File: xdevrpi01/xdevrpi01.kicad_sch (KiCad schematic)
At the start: 20 parts

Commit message: xdevrpi01
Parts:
- removed C?: 22uF, symbol Device:C
- removed U?: AMS1117-3.3, Package_TO_SOT_SMD:SOT-223-3_TabPin2, symbol Regulator_Linear:AMS1117-3.3
- added C1, C2: 15pF, Capacitor_SMD:C_0402_1005Metric, symbol Device:C
- added C3, C4, C5: 100nF, Capacitor_SMD:C_0402_1005Metric, symbol Device:C
- added C6, C7: 1uF, Capacitor_SMD:C_0402_1005Metric, symbol Device:C
- added D1: LED, LED_SMD:LED_0603_1608Metric, symbol Device:LED
- added R1, R2: 27, Resistor_SMD:R_0402_1005Metric, symbol Device:R
- added R3, R4, R6: 1k, Resistor_SMD:R_0402_1005Metric, symbol Device:R
- added R5, R9: 10k, Resistor_SMD:R_0402_1005Metric, symbol Device:R
- added SW1: BOOT, tactile_switches:TS-1088-AR02016, symbol Switch:SW_Push
- added SW2: RST, tactile_switches:TS-1088-AR02016, symbol Switch:SW_Push
- added U1: AP2112K-3.3, Package_TO_SOT_SMD:SOT-23-5, symbol Regulator_Linear:AP2112K-3.3
- added U4: Feather, adafruit:Feather_Main, symbol adafruit:Feather
- added Y1: 12MHz, Crystal:Crystal_SMD_3225-4Pin_3.2x2.5mm, symbol Device:Crystal_GND24
- C10, C11, C12, C13, C14, C15, C16, C8, C9: renamed from C?; footprint (none) -> Capacitor_SMD:C_0402_1005Metric; LCSC (none) -> C307331
- C17, C18: renamed from C?; footprint (none) -> Capacitor_SMD:C_0402_1005Metric; LCSC (none) -> C52923
- D2, D3: renamed from D?; footprint (none) -> LED_SMD:LED_0603_1608Metric; LCSC (none) -> C72043
- P1: renamed from P?; footprint (none) -> USB-C-Connectors:TYPE-C-31-M-04; LCSC (none) -> C129018
- R7: renamed from R?; value 2k -> 1k; footprint (none) -> Resistor_SMD:R_0402_1005Metric; LCSC (none) -> C25543
- R8: renamed from R?; footprint (none) -> Resistor_SMD:R_0402_1005Metric; LCSC (none) -> C25543
- U2: renamed from U?; LCSC (none) -> C2040
- U3: renamed from U?; LCSC (none) -> C97521
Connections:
- net +3V3: now also U2.43 (ADC_AVDD), U2.48 (USB_VDD), C3.1, C7.1, R5.1, U1.5 (VOUT), U4.14 (VCC); no longer C17.1, U2.44 (VREG_VIN)
- net GND: now also C1.1, C2.1, C3.2, C4.2, C5.2, C6.2, C7.2, R6.2, SW1.1, SW2.2, U1.2 (GND), U4.16 (GND), Y1.2, Y1.4
- net VBUS: now also R9.1, U1.1 (VIN), U4.3 (VBUS)
- net usb_dm: now also R1.1
- net usb_dp: now also R2.1
- net at U3.1 (~{CS}): now also U2.56 (QSPI_SS_N), R4.2
- net at U3.2 (DO(IO1)): now also U2.55 (QSPI_SD1)
- net at U3.3 (IO2): now also U2.54 (QSPI_SD2)
- net at U3.5 (DI(IO0)): now also U2.53 (QSPI_SD0)
- net at U3.6 (CLK): now also U2.52 (QSPI_SCLK)
- net at U3.7 (IO3): now also U2.51 (QSPI_SD3)
- net uart_tx: now reaches U2.11 (GPIO8)
- net uart_tx: now also U4.27 (D1)
- net uart_rx: now reaches U2.12 (GPIO9)
- net uart_rx: now also U4.26 (D0)
- net sda: now reaches U2.13 (GPIO10)
- net sda: now also U4.12 (SDA)
- net scl: now reaches U2.14 (GPIO11)
- net scl: now also U4.11 (SCL)
- net sck: now reaches U2.17 (GPIO14)
- net sck: now also U4.23 (SCK)
- net mosi: now reaches U2.18 (GPIO15)
- net mosi: now also U4.24 (MOSI)
- net d2: now reaches U2.2 (GPIO0)
- net d2: now also U4.28 (D2)
- net xin: now reaches U2.20 (XIN)
- net xin: now also C1.2, Y1.1
- net xout: now reaches U2.21 (XOUT)
- net xout: now also R3.2
- net +1V1: now reaches U2.23 (DVDD), U2.45 (VREG_VOUT), U2.50 (DVDD)
- net +1V1: now also C17.1, U2.44 (VREG_VIN), C4.1, C5.1, C6.1
- net swclk: now reaches U2.24 (SWCLK)
- net swclk: now also U4.21 (A4)
- net swdio: now reaches U2.25 (SWDIO)
- net swdio: now also U4.20 (A3)
- net run: now reaches U2.26 (RUN)
- net run: now also R5.2, SW2.1, U4.13 (~{RESET})
- net miso: now reaches U2.27 (GPIO16)
- net miso: now also U4.25 (MISO)
- net d5: now reaches U2.3 (GPIO1)
- net d5: now also U4.10 (D5)
- net a0: now reaches U2.38 (GPIO26/ADC0)
- net a0: now also U4.17 (A0)
- net a1: now reaches U2.39 (GPIO27/ADC1)
- net a1: now also U4.18 (A1)
- net d6: now reaches U2.4 (GPIO2)
- net d6: now also U4.9 (D6)
- net a2: now reaches U2.40 (GPIO28/ADC2)
- net a2: now also U4.19 (A2)
- net a3: now reaches U2.41 (GPIO29/ADC3)
- net at U2.46 (USB_DM): now also R1.2
- net at U2.47 (USB_DP): now also R2.2
- net d10: now reaches U2.5 (GPIO3)
- net d10: now also U4.7 (D10)
- net d11: now reaches U2.6 (GPIO4)
- net d11: now also U4.6 (D11)
- net d12: now reaches U2.7 (GPIO5)
- net d12: now also U4.5 (D12)
- net d13: now reaches U2.8 (GPIO6)
- net d13: now also U4.4 (D13)
- net at U2.9 (GPIO7): now also D1.2 (A)
- new net: D1.1 (K), R6.1
- new net: C2.2, R3.1, Y1.3
- new net: R4.1, SW1.2
- new net: R9.2, U1.3 (EN)
- new net d9: U4.8 (D9)
- no-connect marks 2 -> 6
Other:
- note added: "These termination resistors should be closed to the RP2040"
- title: (none) -> RP2040 Dev board
- moved on the sheet: C17, C18, P1, U2, U3

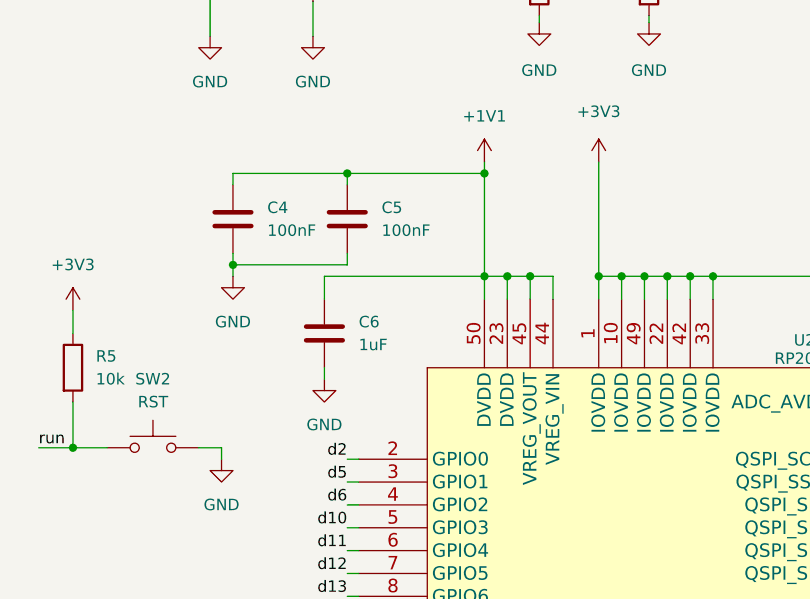
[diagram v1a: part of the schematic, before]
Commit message: fix regulator pin
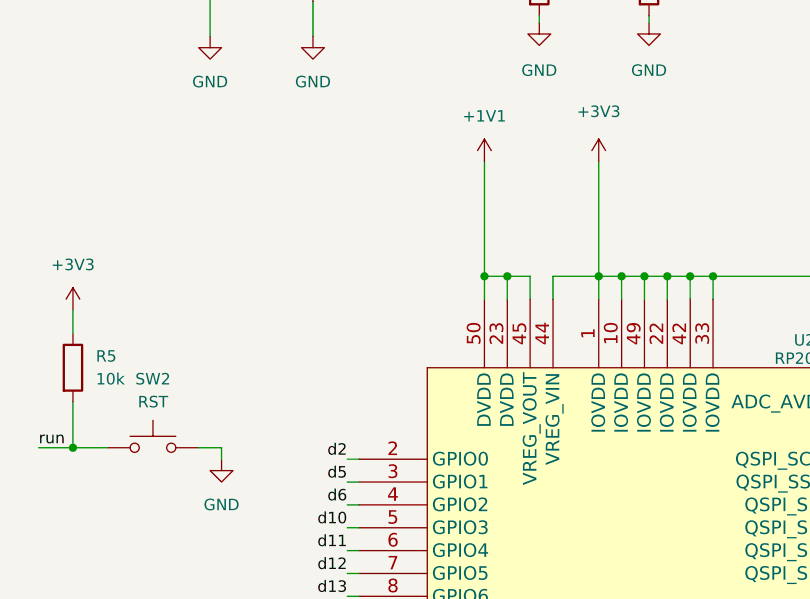
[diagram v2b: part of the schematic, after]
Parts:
- removed C4, C5: 100nF, Capacitor_SMD:C_0402_1005Metric, symbol Device:C
- removed C6: 1uF, Capacitor_SMD:C_0402_1005Metric, symbol Device:C
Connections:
- net +1V1: no longer U2.44 (VREG_VIN)
- net +3V3: now also U2.44 (VREG_VIN)
